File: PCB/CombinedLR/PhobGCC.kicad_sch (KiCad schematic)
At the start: 74 parts, among them J2 Conn_01x04_Female, J3 Conn_01x01_Male, J4 Conn_01x04_Male, J5 Conn_01x02_Male, Q1 Q_NMOS_GSD, Q2 Q_PMOS_GDS, Q3 Q_NMOS_GSD, SW1 A, SW10 Dup, SW11 Dright, SW12 Ddown, SW2 B, SW3 X, SW4 Y, SW5 Start, SW6 L, SW7 R, SW9 Dleft, U1 Teensy4.0, U2 2x DRV5053CAQLPGM Hall Effect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, U3 GP2S60-MFG, U4 GP2S60-MFG, U5 Stickbox_Assembly

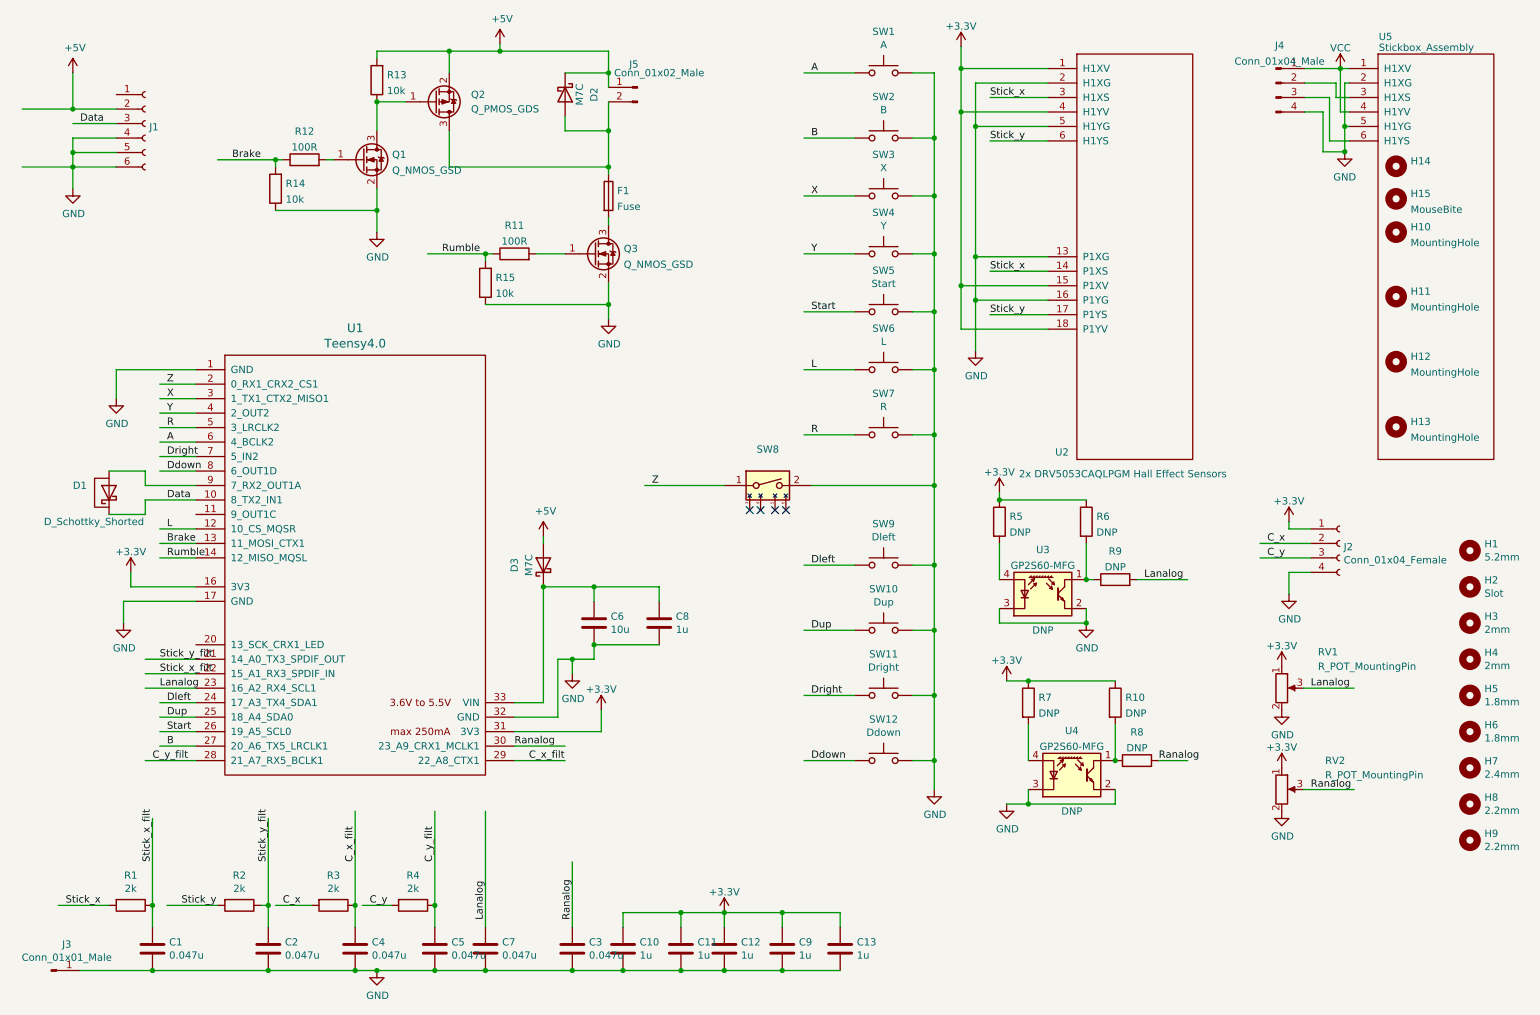
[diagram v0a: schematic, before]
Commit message: fixed LR
working on mouseclick LR boards.
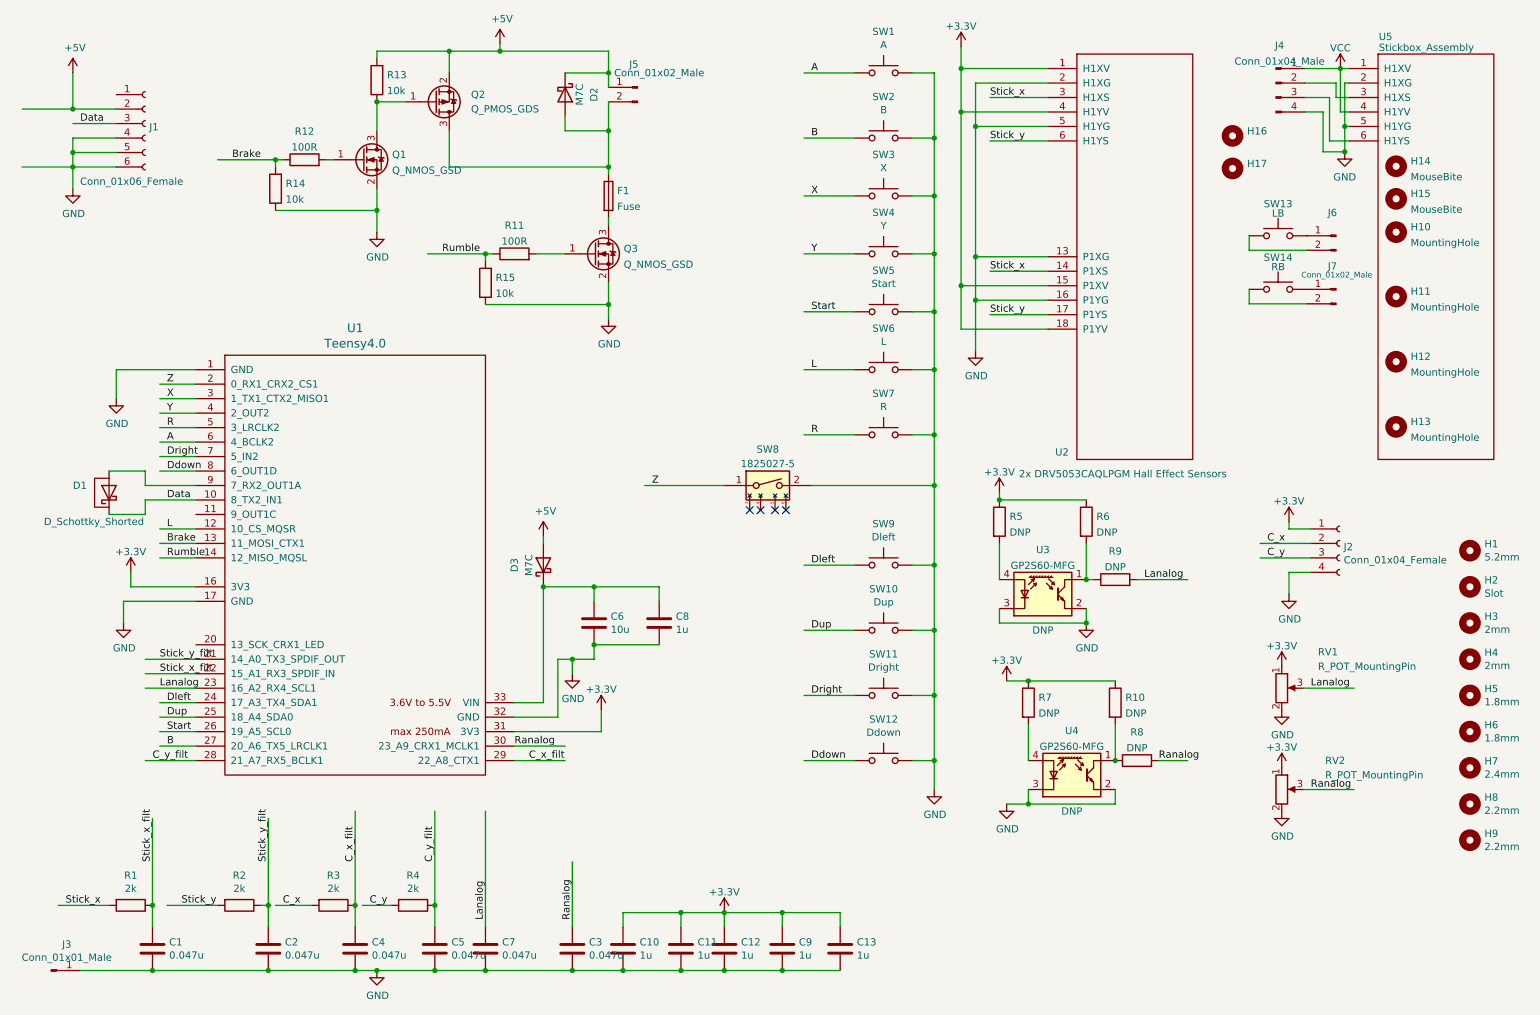
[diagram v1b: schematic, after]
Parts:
- added H16, H17: (no value), symbol Mechanical:MountingHole
- added J6: (no value), Connector_PinHeader_2.54mm:PinHeader_1x02_P2.54mm_Vertical, symbol Connector:Conn_01x02_Male
- added J7: Conn_01x02_Male, Connector_PinHeader_2.54mm:PinHeader_1x02_P2.54mm_Vertical, symbol Connector:Conn_01x02_Male
- added SW13: LB, PhobGCC_Footprints:Trigger_Contact, symbol Switch:SW_Push
- added SW14: RB, PhobGCC_Footprints:Trigger_Contact, symbol Switch:SW_Push
- H14: value (none) -> MouseBite; footprint (none) -> PhobGCC_Footprints:mouse-bite-2.54mm-slot
- H15: footprint (none) -> PhobGCC_Footprints:mouse-bite-2.54mm-slot
- J1: value (none) -> Conn_01x06_Female; footprint (none) -> PhobGCC_Footprints:GCC_Header_Straight_1x06_Pitch2.00mm
- SW8: value (none) -> 1825027-5; footprint (none) -> PhobGCC_Footprints:Z_Switch_Edge
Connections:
- new net: J6.1 (Pin_1), SW13.1
- new net: J6.2 (Pin_2), SW13.2
- new net: J7.1 (Pin_1), SW14.1
- new net: J7.2 (Pin_2), SW14.2
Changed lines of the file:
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@@
     (stroke (width 0) (type default) (color 0 0 0 0))
   )
+  (wire (pts (xy 233.045 53.975) (xy 243.205 53.975))
+    (stroke (width 0) (type default) (color 0 0 0 0))
+  )
   (wire (pts (xy 113.03 140.97) (xy 104.14 140.97))
     (stroke (width 0) (type default) (color 0 0 0 0))
@@
     (stroke (width 0) (type default) (color 0 0 0 0))
   )
+  (wire (pts (xy 233.045 60.833) (xy 233.045 63.373))
+    (stroke (width 0) (type default) (color 0 0 0 0))
+  )
   (wire (pts (xy 114.3 125.73) (xy 114.3 128.27))
     (stroke (width 0) (type default) (color 0 0 0 0))
@@
     (stroke (width 0) (type default) (color 0 0 0 0))
   )
+  (wire (pts (xy 233.045 63.373) (xy 243.205 63.373))
+    (stroke (width 0) (type default) (color 0 0 0 0))
+  )
   (wire (pts (xy 249.809 32.258) (xy 250.571 32.258))
     (stroke (width 0) (type default) (color 0 0 0 0))
@@
     (stroke (width 0) (type default) (color 0 0 0 0))
   )
+  (wire (pts (xy 233.045 51.435) (xy 233.045 53.975))
+    (stroke (width 0) (type default) (color 0 0 0 0))
+  )
   (wire (pts (xy 101.6 17.78) (xy 101.6 19.05))
     (stroke (width 0) (type default) (color 0 0 0 0))
@@
       (effects (font (size 1.27 1.27)) (justify left))
     )
-    (property "Value" "" (id 1) (at 27.94 41.91 0)
+    (property "Value" "Conn_01x06_Female" (id 1) (at 27.94 41.91 0)
       (effects (font (size 1.27 1.27)) (justify left))
     )
-    (property "Footprint" "" (id 2) (at 39.37 31.75 0)
+    (property "Footprint" "PhobGCC_Footprints:GCC_Header_Straight_1x06_Pitch2.00mm" (id 2) (at 39.37 31.75 0)
       (effects (font (size 1.27 1.27)) hide)
     )
@@
     (in_bom yes) (on_board yes)
     (property "Reference" "SW8" (id 0) (at 148.59 88.9 0))
-    (property "Value" "" (id 1) (at 148.59 91.44 0))
-    (property "Footprint" "" (id 2) (at 148.59 95.25 0)
+    (property "Value" "1825027-5" (id 1) (at 148.59 91.44 0))
+    (property "Footprint" "PhobGCC_Footprints:Z_Switch_Edge" (id 2) (at 148.59 95.25 0)
       (effects (font (size 1.27 1.27)) hide)
     )
@@
     (pin "1")
   )
+  (symbol (lib_id "Connector:Conn_01x02_Male") (at 248.285 51.435 0) (mirror y) (unit 1)
+    (in_bom yes) (on_board yes)
+    (property "Reference" "J6" (id 0) (at 247.65 47.3923 0))
+    (property "Value" "" (id 1) (at 248.412 48.895 0)
+      (effects (font (size 1 1)))
+    )
+    (property "Footprint" "Connector_PinHeader_2.54mm:PinHeader_1x02_P2.54mm_Vertical" (id 2) (at 248.285 51.435 0)
+      (effects (font (size 1.27 1.27)) hide)
+    )
+    (property "Datasheet" "~" (id 3) (at 248.285 51.435 0)
+      (effects (font (size 1.27 1.27)) hide)
+    )
+    (pin "1")
+    (pin "2")
+  )
   (symbol (lib_id "power:VCC") (at 249.047 22.098 0) (unit 1)
     (in_bom yes) (on_board yes)
@@
     (pin "2")
   )
+  (symbol (lib_id "Connector:Conn_01x02_Male") (at 248.285 60.833 0) (mirror y) (unit 1)
+    (in_bom yes) (on_board yes)
+    (property "Reference" "J7" (id 0) (at 247.65 56.7903 0))
+    (property "Value" "Conn_01x02_Male" (id 1) (at 248.412 58.293 0)
+      (effects (font (size 1 1)))
+    )
+    (property "Footprint" "Connector_PinHeader_2.54mm:PinHeader_1x02_P2.54mm_Vertical" (id 2) (at 248.285 60.833 0)
+      (effects (font (size 1.27 1.27)) hide)
+    )
+    (property "Datasheet" "~" (id 3) (at 248.285 60.833 0)
+      (effects (font (size 1.27 1.27)) hide)
+    )
+    (pin "1")
+    (pin "2")
+  )
   (symbol (lib_id "Device:Fuse") (at 120.65 44.45 0) (unit 1)
     (in_bom yes) (on_board yes) (fields_autoplaced)
@@
       (effects (font (size 1.27 1.27)) (justify left))
     )
-    (property "Value" "" (id 1) (at 261.366 41.1096 0)
+    (property "Value" "MouseBite" (id 1) (at 261.366 41.1096 0)
       (effects (font (size 1.27 1.27)) (justify left))
     )
-    (property "Footprint" "" (id 2) (at 258.826 39.243 0)
+    (property "Footprint" "PhobGCC_Footprints:mouse-bite-2.54mm-slot" (id 2) (at 258.826 39.243 0)
       (effects (font (size 1.27 1.27)) hide)
     )
@@
     (pin "4")
   )
+  (symbol (lib_id "Mechanical:MountingHole") (at 230.124 33.909 0) (unit 1)
+    (in_bom yes) (on_board yes) (fields_autoplaced)
+    (property "Reference" "H16" (id 0) (at 232.664 33.0743 0)
+      (effects (font (size 1.27 1.27)) (justify left))
+    )
+    (property "Value" "" (id 1) (at 232.664 35.6112 0)
+      (effects (font (size 1.27 1.27)) (justify left))
+    )
+    (property "Footprint" "" (id 2) (at 230.124 33.909 0)
+      (effects (font (size 1.27 1.27)) hide)
+    )
+    (property "Datasheet" "~" (id 3) (at 230.124 33.909 0)
+      (effects (font (size 1.27 1.27)) hide)
+    )
+  )
   (symbol (lib_id "Sensor_Proximity:BPR-105") (at 201.93 146.05 0) (unit 1)
     (in_bom yes) (on_board yes)
@@
     )
   )
+  (symbol (lib_name "SW_Push_2") (lib_id "Switch:SW_Push") (at 238.125 60.833 0) (unit 1)
+    (in_bom yes) (on_board yes)
+    (property "Reference" "SW14" (id 0) (at 238.125 55.245 0))
+    (property "Value" "RB" (id 1) (at 238.125 56.896 0))
+    (property "Footprint" "PhobGCC_Footprints:Trigger_Contact" (id 2) (at 238.125 55.753 0)
+      (effects (font (size 1.27 1.27)) hide)
+    )
+    (property "Datasheet" "~" (id 3) (at 238.125 55.753 0)
+      (effects (font (size 1.27 1.27)) hide)
+    )
+    (pin "1")
+    (pin "2")
+  )
   (symbol (lib_id "Device:R") (at 104.14 54.61 90) (unit 1)
     (in_bom yes) (on_board yes) (fields_autoplaced)
@@
     (pin "2")
   )
+  (symbol (lib_id "Mechanical:MountingHole") (at 230.124 39.624 0) (unit 1)
+    (in_bom yes) (on_board yes) (fields_autoplaced)
+    (property "Reference" "H17" (id 0) (at 232.664 38.7893 0)
+      (effects (font (size 1.27 1.27)) (justify left))
+    )
+    (property "Value" "" (id 1) (at 232.664 41.3262 0)
+      (effects (font (size 1.27 1.27)) (justify left))
+    )
+    (property "Footprint" "" (id 2) (at 230.124 39.624 0)
+      (effects (font (size 1.27 1.27)) hide)
+    )
+    (property "Datasheet" "~" (id 3) (at 230.124 39.624 0)
+      (effects (font (size 1.27 1.27)) hide)
+    )
+  )
   (symbol (lib_id "power:GND") (at 249.809 36.703 0) (unit 1)
     (in_bom yes) (on_board yes) (fields_autoplaced)
@@
     (pin "1")
   )
+  (symbol (lib_name "SW_Push_1") (lib_id "Switch:SW_Push") (at 238.125 51.435 0) (unit 1)
+    (in_bom yes) (on_board yes)
+    (property "Reference" "SW13" (id 0) (at 238.125 45.847 0))
+    (property "Value" "LB" (id 1) (at 238.125 47.498 0))
+    (property "Footprint" "PhobGCC_Footprints:Trigger_Contact" (id 2) (at 238.125 46.355 0)
+      (effects (font (size 1.27 1.27)) hide)
+    )
+    (property "Datasheet" "~" (id 3) (at 238.125 46.355 0)
+      (effects (font (size 1.27 1.27)) hide)
+    )
+    (pin "1")
+    (pin "2")
+  )
   (symbol (lib_id "Device:C") (at 118.11 119.38 0) (unit 1)
     (in_bom yes) (on_board yes)
@@
       (effects (font (size 1.27 1.27)) (justify left))
     )
-    (property "Footprint" "" (id 2) (at 258.826 44.958 0)
+    (property "Footprint" "PhobGCC_Footprints:mouse-bite-2.54mm-slot" (id 2) (at 258.826 44.958 0)
       (effects (font (size 1.27 1.27)) hide)
     )
@@
       (reference "H15") (unit 1) (value "MouseBite") (footprint "PhobGCC_Footprints:mouse-bite-2.54mm-slot")
     )
+    (path "/cee780b2-d029-4e98-8379-2557c9e148e3"
+      (reference "H16") (unit 1) (value "MouseBiteLB") (footprint "PhobGCC_Footprints:breakaway-mousebites")
+    )
+    (path "/df2bc5b1-8420-4d9c-936b-e42e3b416681"
+      (reference "H17") (unit 1) (value "MouseBiteRB") (footprint "PhobGCC_Footprints:breakaway-mousebites")
+    )
     (path "/00000000-0000-0000-0000-000061572882"
       (reference "J1") (unit 1) (value "Conn_01x06_Female") (footprint "PhobGCC_Footprints:GCC_Header_Straight_1x06_Pitch2.00mm")
@@
       (reference "J5") (unit 1) (value "Conn_01x02_Male") (footprint "Connector_PinHeader_2.54mm:PinHeader_1x02_P2.54mm_Vertical")
     )
+    (path "/1d5d6693-eda1-423e-a563-7a2114f51108"
+      (reference "J6") (unit 1) (value "Conn_01x02_Male") (footprint "Connector_PinHeader_2.54mm:PinHeader_1x02_P2.54mm_Vertical")
+    )
+    (path "/43e186f4-4d59-4a50-bef4-ff753ba9e923"
+      (reference "J7") (unit 1) (value "Conn_01x02_Male") (footprint "Connector_PinHeader_2.54mm:PinHeader_1x02_P2.54mm_Vertical")
+    )
     (path "/d2da7f57-ee9e-4fd2-ab66-6ced21a875ef"
       (reference "Q1") (unit 1) (value "Q_NMOS_GSD") (footprint "Package_TO_SOT_SMD:SOT-23")
@@
       (reference "SW12") (unit 1) (value "Ddown") (footprint "PhobGCC_Footprints:Dpad_Contact_TL3315NF_2")
     )
+    (path "/ecab30c4-546c-46da-8332-d218e09ac3ff"
+      (reference "SW13") (unit 1) (value "LB") (footprint "PhobGCC_Footprints:Trigger_Contact")
+    )
+    (path "/da06455a-cfd6-4278-a2c0-9c38c8567165"
+      (reference "SW14") (unit 1) (value "RB") (footprint "PhobGCC_Footprints:Trigger_Contact")
+    )
     (path "/00000000-0000-0000-0000-00006154c933"
